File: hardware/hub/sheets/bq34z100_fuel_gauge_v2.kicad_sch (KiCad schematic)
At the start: 6 parts, among them J401 S2B-ZR, U3 BQ34Z100PWR-G1

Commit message: Clamp Q2's gate so the DC input can run to the charger's full 24 V
The solar/DC reverse-polarity FET Q2 is self-biased: its gate sits at ground
through R19, so the full input voltage appears across the gate oxide. That is
true in normal operation, not only under a reversed source - a correctly
connected 24 V panel stresses the gate exactly as hard as a backwards one. The
DMP3098L-7's +/-20 V gate rating therefore capped the usable input at 20 V,
below the 24 V the BQ25798 itself accepts. The protection, not the charger, was
setting the ceiling.

D2 (BZT52C12S, 12 V zener, LCSC C19077447) clamps gate-to-source: cathode to
the source at CN5 pin 1, anode to the gate. Above roughly 12 V in it holds Vgs
near -12 V; reversed, it holds it near +0.7 V. R19 stays at 100 kOhm, giving
120 uA of clamp current at 24 V in - deliberately below the zener's 5 mA test
current, since reaching the knee would need R19 near 2.4 kOhm and draw 5 mA
continuously from the panel.

Also carries the PCB v2 IC and passive validation work: the ship-FET addition,
the PWR_FLAGs that resolve the power_pin_not_driven ERC entries, and the
charger, fuel-gauge, regulator and I2C-buffer sheet updates documented
alongside them.

Tooling, alongside the design change:

  - tools/run_kicad_validation.sh called tools/validation/check_violations.py
    with known_exceptions.json. Neither file has ever been committed, so the
    local pre-flight failed on every run since the initial commit. It now calls
    tools/check_erc_baseline.py against erc-baseline.json, mirroring
    .github/workflows/validate-hardware.yml - errors only, and DRC gains
    --refill-zones and --exit-code-violations. CI was never affected.
  - The ERC baseline is now empty. All five accepted entries were
    power_pin_not_driven, and the PWR_FLAGs resolve every one. An empty
    baseline is stricter: nothing is absorbed by a matching entry any more.
  - Ignore hardware/hub/jlcpcb/, the kicad-jlcpcb-tools plugin's parts cache.

Verified: th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
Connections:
- net VBAT renamed VBAT_PROTECTED
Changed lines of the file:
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@@
+	)
+	(junction
+		(at 224.79 236.22)
+		(diameter 0)
+		(color 0 0 0 0)
+	)
+	(junction
+		(at 224.79 232.41)
+		(diameter 0)
+		(color 0 0 0 0)
+	)
+	(junction
+		(at 283.21 241.3)
+		(diameter 0)
+		(color 0 0 0 0)
 	)
 	(junction
@@
 	(wire
 		(pts
-			(xy 275.59 241.3) (xy 285.75 241.3)
+			(xy 275.59 241.3) (xy 283.21 241.3)
+		)
+		(stroke
+			(width 0)
+			(type default)
+		)
+	)
+	(wire
+		(pts
+			(xy 283.21 241.3) (xy 285.75 241.3)
 		)
 		(stroke
@@
 	(wire
 		(pts
+			(xy 224.79 236.22) (xy 224.79 241.3)
+		)
+		(stroke
+			(width 0)
+			(type default)
+		)
+	)
+	(wire
+		(pts
+			(xy 224.79 231.14) (xy 224.79 232.41)
+		)
+		(stroke
+			(width 0)
+			(type default)
+		)
+	)
+	(wire
+		(pts
 			(xy 234.95 231.14) (xy 224.79 231.14)
 		)
@@
 		(pts
 			(xy 234.95 241.3) (xy 224.79 241.3)
+		)
+		(stroke
+			(width 0)
+			(type default)
+		)
+	)
+	(wire
+		(pts
+			(xy 224.79 232.41) (xy 224.79 236.22)
 		)
 		(stroke
@@
 		)
 	)
-	(global_label "VBAT"
+	(global_label "SCL_INT"
 		(shape input)
-		(at 224.79 236.22 180)
+		(at 285.75 215.9 0)
 		(fields_autoplaced yes)
 		(effects
@@
 				(size 1.27 1.27)
 			)
-			(justify right)
+			(justify left)
 		)
 		(property "Intersheetrefs" "${INTERSHEET_REFS}"
-			(at 217.39 236.22 0)
-			(hide yes)
-			(show_name no)
-			(do_not_autoplace no)
-			(effects
-				(font
-					(size 1.27 1.27)
-				)
-				(justify right)
-			)
-		)
-	)
-	(global_label "SCL_INT"
+			(at 296.1133 215.9 0)
+			(hide yes)
+			(show_name no)
+			(do_not_autoplace no)
+			(effects
+				(font
+					(size 1.27 1.27)
+				)
+				(justify left)
+			)
+		)
+	)
+	(global_label "VBAT_PROTECTED"
 		(shape input)
-		(at 285.75 215.9 0)
+		(at 182.88 189.23 270)
 		(fields_autoplaced yes)
 		(effects
@@
 				(size 1.27 1.27)
 			)
-			(justify left)
+			(justify right)
 		)
 		(property "Intersheetrefs" "${INTERSHEET_REFS}"
-			(at 296.1133 215.9 0)
-			(hide yes)
-			(show_name no)
-			(do_not_autoplace no)
-			(effects
-				(font
-					(size 1.27 1.27)
-				)
-				(justify left)
+			(at 182.88 208.2413 90)
+			(hide yes)
+			(show_name no)
+			(do_not_autoplace no)
+			(effects
+				(font
+					(size 1.27 1.27)
+				)
+				(justify right)
 			)
 		)
@@
 		)
 	)
+	(global_label "VBAT_PROTECTED"
+		(shape input)
+		(at 224.79 236.22 180)
+		(fields_autoplaced yes)
+		(effects
+			(font
+				(size 1.27 1.27)
+			)
+			(justify right)
+		)
+		(property "Intersheetrefs" "${INTERSHEET_REFS}"
+			(at 205.7787 236.22 0)
+			(hide yes)
+			(show_name no)
+			(do_not_autoplace no)
+			(effects
+				(font
+					(size 1.27 1.27)
+				)
+				(justify right)
+			)
+		)
+	)
 	(global_label "SDA_INT"
 		(shape input)
@@
 		)
 	)
-	(global_label "VBAT"
+	(global_label "FG_SRN"
 		(shape input)
-		(at 224.79 231.14 180)
+		(at 285.75 226.06 0)
 		(fields_autoplaced yes)
 		(effects
@@
 				(size 1.27 1.27)
 			)
-			(justify right)
-		)
-		(property "Intersheetrefs" "${INTERSHEET_REFS}"
-			(at 217.39 231.14 0)
-			(hide yes)
-			(show_name no)
-			(do_not_autoplace no)
-			(effects
-				(font
-					(size 1.27 1.27)
-				)
-				(justify right)
-			)
-		)
-	)
-	(global_label "VBAT"
-		(shape input)
-		(at 182.88 189.23 270)
-		(fields_autoplaced yes)
-		(effects
-			(font
-				(size 1.27 1.27)
-			)
-			(justify right)
-		)
-		(property "Intersheetrefs" "${INTERSHEET_REFS}"
-			(at 182.88 196.63 90)
-			(hide yes)
-			(show_name no)
-			(do_not_autoplace no)
-			(effects
-				(font
-					(size 1.27 1.27)
-				)
-				(justify right)
-			)
-		)
-	)
-	(global_label "FG_SRN"
-		(shape input)
-		(at 285.75 226.06 0)
-		(fields_autoplaced yes)
-		(effects
-			(font
-				(size 1.27 1.27)
-			)
 			(justify left)
 		)
@@
 				)
 				(justify left)
-			)
-		)
-	)
-	(global_label "VBAT"
-		(shape input)
-		(at 224.79 241.3 180)
-		(fields_autoplaced yes)
-		(effects
-			(font
-				(size 1.27 1.27)
-			)
-			(justify right)
-		)
-		(property "Intersheetrefs" "${INTERSHEET_REFS}"
-			(at 217.39 241.3 0)
-			(hide yes)
-			(show_name no)
-			(do_not_autoplace no)
-			(effects
-				(font
-					(size 1.27 1.27)
-				)
-				(justify right)
 			)
 		)
@@
 	)
 	(symbol
+		(lib_id "power:PWR_FLAG")
+		(at 283.21 241.3 0)
+		(unit 1)
+		(body_style 1)
+		(exclude_from_sim no)
+		(in_bom yes)
+		(on_board yes)
+		(in_pos_files yes)
+		(dnp no)
+		(fields_autoplaced yes)
+		(property "Reference" "#FLG010"
+			(at 283.21 239.395 0)
+			(hide yes)
+			(show_name no)
+			(do_not_autoplace no)
+			(effects
+				(font
+					(size 1.27 1.27)
+				)
+			)
+		)
+		(property "Value" "PWR_FLAG"
+			(at 283.21 236.22 0)
+			(show_name no)
+			(do_not_autoplace no)
+			(effects
+				(font
+					(size 1.27 1.27)
+				)
+			)
+		)
+		(property "Footprint" ""
+			(at 283.21 241.3 0)
+			(hide yes)
+			(show_name no)
+			(do_not_autoplace no)
+			(effects
+				(font
+					(size 1.27 1.27)
+				)
+			)
+		)
+		(property "Datasheet" ""
+			(at 283.21 241.3 0)
+			(hide yes)
+			(show_name no)
+			(do_not_autoplace no)
+			(effects
+				(font
+					(size 1.27 1.27)
+				)
+			)
+		)
+		(property "Description" "Special symbol for telling ERC where power comes from"
+			(at 283.21 241.3 0)
+			(hide yes)
+			(show_name no)
+			(do_not_autoplace no)
+			(effects
+				(font
+					(size 1.27 1.27)
+				)
+			)
+		)
+		(pin "1"
+		)
+		(instances
+			(project "SunSproutHub"
+				(path "/a73062bd-90e7-442f-aac6-ee7677f83b11/3a0e399f-7a0a-4d50-8ecb-e7abcc14a097"
+					(reference "#FLG010")
+					(unit 1)
+				)
+			)
+		)
+	)
+	(symbol
 		(lib_id "PCM_SparkFun-Connector:TestPoint_1.0mm")
 		(at 299.72 189.23 180)
@@
 					(unit 1)
 				)
+			)
+		)
+	)
+	(symbol
+		(lib_id "power:PWR_FLAG")
+		(at 224.79 232.41 90)
+		(unit 1)
+		(body_style 1)
+		(exclude_from_sim no)
+		(in_bom yes)
+		(on_board yes)
+		(in_pos_files yes)
+		(dnp no)
+		(fields_autoplaced yes)
+		(property "Reference" "#FLG09"
+			(at 222.885 232.41 0)
+			(hide yes)
+			(show_name no)
+			(do_not_autoplace no)
+			(effects
+				(font
+					(size 1.27 1.27)
+				)
+			)
+		)
+		(property "Value" "PWR_FLAG"
+			(at 220.98 232.4099 90)
+			(show_name no)
+			(do_not_autoplace no)
+			(effects
+				(font
+					(size 1.27 1.27)
+				)
+				(justify left)
+			)
+		)
+		(property "Footprint" ""
+			(at 224.79 232.41 0)
+			(hide yes)
+			(show_name no)
+			(do_not_autoplace no)
+			(effects
+				(font
+					(size 1.27 1.27)
+				)
+			)
+		)
+		(property "Datasheet" ""
+			(at 224.79 232.41 0)
+			(hide yes)
+			(show_name no)
+			(do_not_autoplace no)
+			(effects
+				(font
+					(size 1.27 1.27)
+				)
+			)
+		)
+		(property "Description" "Special symbol for telling ERC where power comes from"
+			(at 224.79 232.41 0)
+			(hide yes)
+			(show_name no)
+			(do_not_autoplace no)
+			(effects
+				(font
+					(size 1.27 1.27)
+				)
+			)
+		)
+		(pin "1"
+		)
+		(instances
+			(project "SunSproutHub"
+				(path "/a73062bd-90e7-442f-aac6-ee7677f83b11/3a0e399f-7a0a-4d50-8ecb-e7abcc14a097"
+					(reference "#FLG09")
+					(unit 1)
+				)

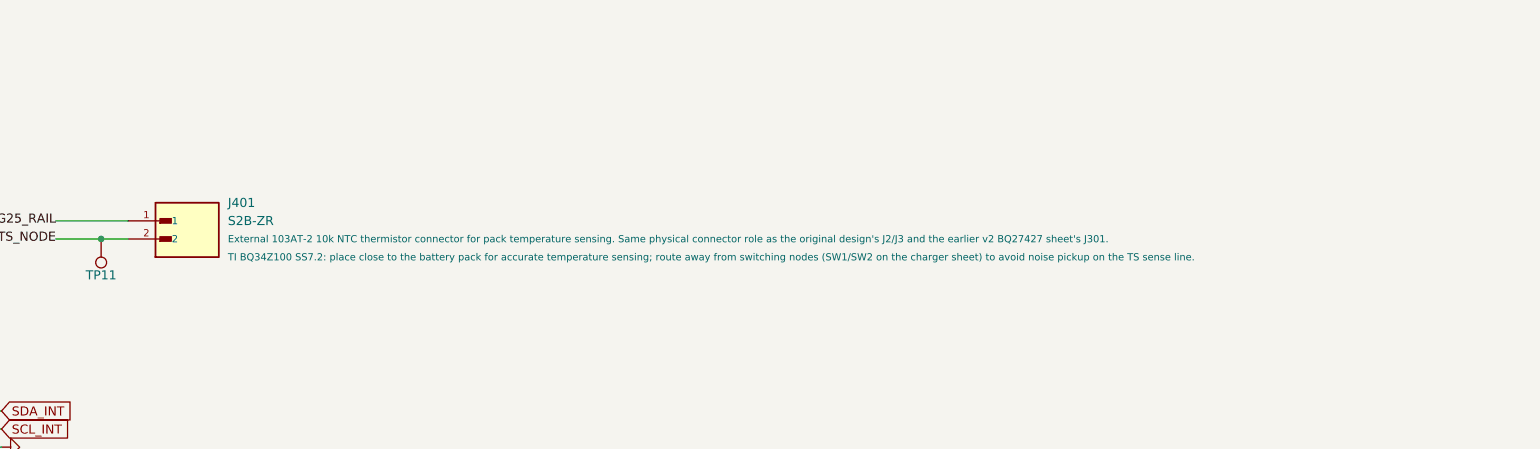
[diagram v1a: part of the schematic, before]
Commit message: Swap thermistor inputs J302/J401 from JST ZH to JST PA
The ZH (S2B-ZR) 1.5 mm housings are impractical to hand-crimp, which
blocks the intended workflow of an end user terminating their own NTC
probe. Move both thermistor inputs to JST PA 2.0 mm side entry
(S02B-PASK-2, LCSC C265094).

Why PA over the alternatives:

- Not PH. J4 (battery input) is already JST PH 2.0 mm; sharing that
  family would let a 4.2 V cell be plugged onto a BQ25798 TS pin.
- Rated -40..+105 C, against -25..+85 C for PH, XH and EH. The connector
  should not be narrower than the range the thermistor qualifies.
- Positive lock. An intermittent TS connection reads as out-of-range and
  suspends charging, so retention matters on a pack-mounted probe.
- 88.9 mm2 courtyard against 105.0 mm2 for XH.

Adds a hand-built footprint for S02B-PASK-2, since none exists in the
stock KiCad libraries. Dimensioned from the JST PA family datasheet
(PC board layout p.3, header dimensions p.9): 2.00 mm pin pitch,
0.7+0.1 mm signal holes, 1.1+0.1 mm NPTH boss holes offset 1.5 mm
outboard of the end pins and 2.1 mm from the pin row, 6.0 x 11.7 mm
body with the pin row 8.2 mm from the mating face.

Docs now specify the Semitec 103AT-11 in place of the 103AT-2. Both are
10 kOhm / B25/85 = 3435 K, but the 103AT-2 ships as a bare bead on 17 mm
solid 42-alloy leads: too short for a crimp barrel, not ductile enough
to form a gas-tight crimp, and with no insulation for the support wings
to grip. The 103AT-11 carries 600 mm of insulated lead. A
solder-to-pigtail fallback is documented for anyone holding 103AT-2
stock, along with a warning that 3D-printer thermistors (100 kOhm,
B ~ 3950) will not work against the 10 kOhm R305/R306 divider.

Also carried here, unrelated to the connector work but coupled to the
same .kicad_pcb: the board's logo footprint moves from
project:Logo-Alternate to project:Logo, with Logo.kicad_mod regenerated.

DRC 0 violations / 0 unconnected; Docusaurus build passes.

Co-Authored-By: Claude Opus 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
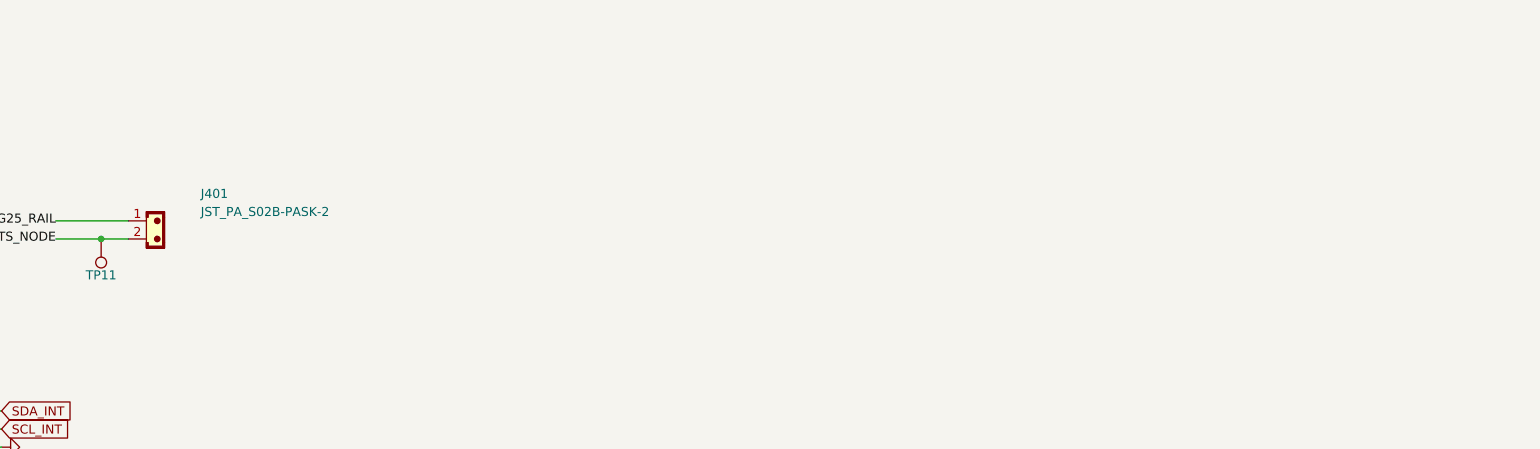
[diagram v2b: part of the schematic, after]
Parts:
- J401: value S2B-ZR -> JST_PA_S02B-PASK-2; footprint Snapeda:JST_S2B-ZR_LF__SN_ -> project:JST_PA_S02B-PASK-2_1x02_P2.00mm_Horizontal; symbol Snapeda:S2B-ZR_LF__SN_ -> project:JST_02; Check_prices https://www.snapeda.com/parts/S2B-ZR%20(LF)(SN)/JST/view-pa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 -> (none); FT Position Offset (none) -> 0,0; FT Rotation Offset (none) -> 0; LCSC Part C157930 -> C265094; MANUFACTURER JST Sales America Inc. -> (none); MAXIMUM_PACKAGE_HEIGHT 3.7mm -> 6.5mm; MF JST Sales -> (none); MP S2B-ZR (LF)(SN) -> (none); MPN S2B-ZR(LF)(SN) -> S02B-PASK-2(LF)(SN); PARTREV NA -> (none); Package None -> (none); STANDARD Manufacturer Recommendations -> (none); SnapEDA_Link https://www.snapeda.com/parts/S2B-ZR%20(LF)(SN)/JST/view-pa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 -> (none); Supplier Part Site (none) -> https://jlcpcb.com/partdetail/JST-S02B_PASK_2_LF_SN/C265094
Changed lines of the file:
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@@
 	)
 	(symbol
-		(lib_id "Snapeda:S2B-ZR_LF__SN_")
-		(at 311.15 189.23 0)
+		(lib_id "project:JST_02")
+		(at 307.34 187.96 0)
 		(unit 1)
 		(body_style 1)
@@
 		(fields_autoplaced yes)
 		(property "Reference" "J401"
-			(at 317.5 184.1499 0)
+			(at 313.69 182.8799 0)
 			(show_name no)
 			(do_not_autoplace no)
@@
 			)
 		)
-		(property "Value" "S2B-ZR"
-			(at 317.5 186.6899 0)
+		(property "Value" "JST_PA_S02B-PASK-2"
+			(at 313.69 185.4199 0)
 			(show_name no)
 			(do_not_autoplace no)
@@
 			)
 		)
-		(property "Footprint" "Snapeda:JST_S2B-ZR_LF__SN_"
-			(at 311.15 189.23 0)
+		(property "Footprint" "project:JST_PA_S02B-PASK-2_1x02_P2.00mm_Horizontal"
+			(at 307.34 187.96 0)
 			(hide yes)
 			(show_name no)
@@
 			)
 		)
-		(property "Datasheet" "https://datasheet.lcsc.com/datasheet/pdf/ea5d0349a6c3a16363d489da6a84290b.pdf?productCode=C157930"
-			(at 311.15 189.23 0)
+		(property "Datasheet" "https://www.jst-mfg.com/product/pdf/eng/ePA-F.pdf"
+			(at 307.34 187.96 0)
 			(hide yes)
 			(show_name no)
@@
 			)
 		)
-		(property "Description" ""
-			(at 311.15 189.23 0)
+		(property "Description" "JST PA 2.00mm side-entry header, 2 circuits, S02B-PASK-2"
+			(at 307.34 187.96 0)
+			(hide yes)
 			(show_name no)
 			(do_not_autoplace no)
@@
 			)
 		)
-		(property "LCSC Part" "C157930"
-			(at 311.15 189.23 0)
+		(property "LCSC Part" "C265094"
+			(at 307.34 187.96 0)
 			(hide yes)
 			(show_name no)
@@
 		)
 		(property "Usage" "External 103AT-2 10k NTC thermistor connector for pack temperature sensing. Same physical connector role as the original design's J2/J3 and the earlier v2 BQ27427 sheet's J301."
-			(at 317.5 189.23 0)
+			(at 313.69 187.96 0)
+			(hide yes)
 			(show_name no)
 			(do_not_autoplace no)
@@
 		)
 		(property "Placement" "TI BQ34Z100 SS7.2: place close to the battery pack for accurate temperature sensing; route away from switching nodes (SW1/SW2 on the charger sheet) to avoid noise pickup on the TS sense line."
-			(at 317.5 191.77 0)
+			(at 313.69 190.5 0)
+			(hide yes)
 			(show_name no)
 			(do_not_autoplace no)
@@
 		)
 		(property "Manufacturer Product Page" ""
-			(at 311.15 189.23 0)
+			(at 307.34 187.96 0)
 			(hide yes)
 			(show_name no)
@@
 		)
 		(property "Supplier" "JLCPCB"
-			(at 311.15 189.23 0)
+			(at 307.34 187.96 0)
 			(hide yes)
 			(show_name no)
@@
 			)
 		)
-		(property "Supplier Part Site" ""
-			(at 311.15 189.23 0)
+		(property "Supplier Part Site" "https://jlcpcb.com/partdetail/JST-S02B_PASK_2_LF_SN/C265094"
+			(at 307.34 187.96 0)
 			(hide yes)
 			(show_name no)
@@
 		)
 		(property "Manufacturer" "JST"
-			(at 1.27 1.27 0)
+			(at -2.54 0 0)
 			(hide yes)
 			(show_name no)
@@
 			)
 		)
-		(property "MPN" "S2B-ZR(LF)(SN)"
-			(at 1.27 1.27 0)
+		(property "MPN" "S02B-PASK-2(LF)(SN)"
+			(at -2.54 0 0)
 			(hide yes)
 			(show_name no)
@@
 			)
 		)
-		(property "DigiKey_Part_Number" ""
-			(at 311.15 189.23 0)
+		(property "MAXIMUM_PACKAGE_HEIGHT" "6.5mm"
+			(at 307.34 187.96 0)
 			(hide yes)
 			(show_name no)
@@
 			)
 		)
-		(property "SnapEDA_Link" "https://www.snapeda.com/parts/S2B-ZR%20(LF)(SN)/JST/view-part/?ref=snap"
-			(at 311.15 189.23 0)
+		(property "FT Rotation Offset" "0"
+			(at 307.34 187.96 0)
 			(hide yes)
 			(show_name no)
@@
 					(size 1.27 1.27)
 				)
-				(justify bottom)
 			)
 		)
-		(property "MAXIMUM_PACKAGE_HEIGHT" "3.7mm"
-			(at 311.15 189.23 0)
+		(property "FT Position Offset" "0,0"
+			(at 307.34 187.96 0)
 			(hide yes)
 			(show_name no)
@@
 					(size 1.27 1.27)
 				)
-				(justify bottom)
 			)
 		)
-		(property "Package" "None"
-			(at 311.15 189.23 0)
-			(hide yes)
-			(show_name no)
-			(do_not_autoplace no)
-			(effects
-				(font
-					(size 1.27 1.27)
-				)
-				(justify bottom)
-			)
-		)
-		(property "Check_prices" "https://www.snapeda.com/parts/S2B-ZR%20(LF)(SN)/JST/view-part/?ref=eda"
-			(at 311.15 189.23 0)
-			(hide yes)
-			(show_name no)
-			(do_not_autoplace no)
-			(effects
-				(font
-					(size 1.27 1.27)
-				)
-				(justify bottom)
-			)
-		)
-		(property "STANDARD" "Manufacturer Recommendations"
-			(at 311.15 189.23 0)
-			(hide yes)
-			(show_name no)
-			(do_not_autoplace no)
-			(effects
-				(font
-					(size 1.27 1.27)
-				)
-				(justify bottom)
-			)
-		)
-		(property "PARTREV" "NA"
-			(at 311.15 189.23 0)
-			(hide yes)
-			(show_name no)
-			(do_not_autoplace no)
-			(effects
-				(font
-					(size 1.27 1.27)
-				)
-				(justify bottom)
-			)
-		)
-		(property "MF" "JST Sales"
-			(at 311.15 189.23 0)
-			(hide yes)
-			(show_name no)
-			(do_not_autoplace no)
-			(effects
-				(font
-					(size 1.27 1.27)
-				)
-				(justify bottom)
-			)
-		)
-		(property "MP" "S2B-ZR (LF)(SN)"
-			(at 311.15 189.23 0)
-			(hide yes)
-			(show_name no)
-			(do_not_autoplace no)
-			(effects
-				(font
-					(size 1.27 1.27)
-				)
-				(justify bottom)
-			)
-		)
-		(property "MANUFACTURER" "JST Sales America Inc."
-			(at 311.15 189.23 0)
-			(hide yes)
-			(show_name no)
-			(do_not_autoplace no)
-			(effects
-				(font
-					(size 1.27 1.27)
-				)
-				(justify bottom)
-			)
-		)

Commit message: Move TS divider R305/R306 to JLCPCB Basic values
R305 5.23k -> 5.1k (C23068 -> C23186) and R306 30.1k -> 30k
(C23000 -> C22984). Both old parts were JLCPCB Extended, carrying
$4.53 each in per-order fees for $0.07 of resistor. The new values
are Basic, and 5.1k is already in the BOM as R5/R6 so R305 adds no
unique part number at all.

Of the 116 Basic/Preferred 0603 resistors in the JLCPCB library,
5.1k/30k is the closest achievable pair to TI's reference network
for a 103AT-type 10k NTC (5.24k/30.31k). The Basic library carries
E24 values only, so the exact E96 values are not available in any
package.

Cost: the JEITA trip points shift about +0.93 C. Against the
documented VT1_RISE of 73.3% of REGN the cold cutoff moves from
roughly +0.97 C to +1.95 C. Both directions are benign for the
LiFePO4 cell this board targets - the cold side errs conservative,
and LiFePO4 tolerates the hot side far better than Li-ion. This is
well inside the VT1 threshold tolerance, which swings the cutoff by
about 3.2 C on its own.

Also updates the values the firmware uses to convert the TS reading
into a temperature. Left stale, ts_resistor_upper/lower would have
reported every cell temperature about 0.85 C low.

Derived constants updated across docs:
  open-circuit divider  85.2% -> 85.5% of REGN
  R306 || 10k NTC @25C  7.506k / 58.9% -> 7.500k / 59.5%

Co-Authored-By: Claude Opus 5 <noreply@anthropic.com>
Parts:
- J401: FT Position Offset 0,0 -> 0,1.01600; FT Rotation Offset 0 -> 180
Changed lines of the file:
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@@
 			)
 		)
-		(property "FT Rotation Offset" "0"
+		(property "FT Rotation Offset" "180"
 			(at 307.34 187.96 0)
 			(hide yes)
@@
 			)
 		)
-		(property "FT Position Offset" "0,0"
+		(property "FT Position Offset" "0,1.01600"
 			(at 307.34 187.96 0)
 			(hide yes)
